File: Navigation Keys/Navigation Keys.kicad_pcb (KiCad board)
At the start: 2 copper layers, 22 parts, among them J1 Conn_01x19_Female, J2 Conn_01x19_Male

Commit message: Started wiring
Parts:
- moved D10 38.1 mm to (199.2, 127.8)
- moved D3 38.1 mm to (161.1, 127.8)
- moved MX_Left1 38.1 mm to (153.2, 127.8)
- moved MX_Right1 38.1 mm to (191.3, 127.8)
- renumbered MX_Right1 to MX_Left1, MX_Left1 to MX_Right1
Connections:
- D10 pad 1: ROW7 -> ROW8
- D3 pad 1: ROW7 -> ROW8
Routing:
- net COL4: track 0.00 -> 94.4 mm, vias 0 -> 8
- net COL5: track 0.00 -> 92.5 mm, vias 0 -> 8
- net GND: track 0.00 -> 85.4 mm, vias 0 -> 10
- net ROW9: track 0.00 -> 83.4 mm, vias 0 -> 8
- net COL6: track 0.00 -> 74.3 mm, vias 0 -> 8
- net COL10: track 0.00 -> 73.4 mm, vias 0 -> 6
- net COL9: track 0.00 -> 72.6 mm, vias 0 -> 6
- net COL7: track 0.00 -> 72.0 mm, vias 0 -> 8
- net COL8: track 0.00 -> 70.3 mm, vias 0 -> 6
- net COL3: track 0.00 -> 57.1 mm
- net COL2: track 0.00 -> 57.1 mm
- net COL1: track 0.00 -> 57.1 mm
- net ROW6: track 0.00 -> 44.5 mm, vias 0 -> 4
- net ROW8: track 0.00 -> 44.5 mm
- net ROW5: track 0.00 -> 44.5 mm, vias 0 -> 4
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
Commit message: Finished wiring and placement
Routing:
- net COL0: track 4.59 -> 108.1 mm, vias 0 -> 10
- net VCC: track 4.75 -> 107.3 mm, vias 0 -> 10
- net ROW8: track 44.5 -> 146.7 mm, vias 0 -> 2
- net +5V: track 4.65 -> 100.3 mm, vias 0 -> 6
- net ROW7: track 0.00 -> 92.9 mm, vias 0 -> 4
- net COL3: track 57.1 -> 148.1 mm, vias 0 -> 6
- net COL2: track 57.1 -> 143.3 mm, vias 0 -> 8
- net COL1: track 57.1 -> 143.1 mm, vias 0 -> 6
- net ROW5: track 44.5 -> 127.3 mm, vias 4 -> 10
- net ROW6: track 44.5 -> 92.9 mm, vias 4 -> 8
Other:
- board outline added: 73.8 x 76.2 mm

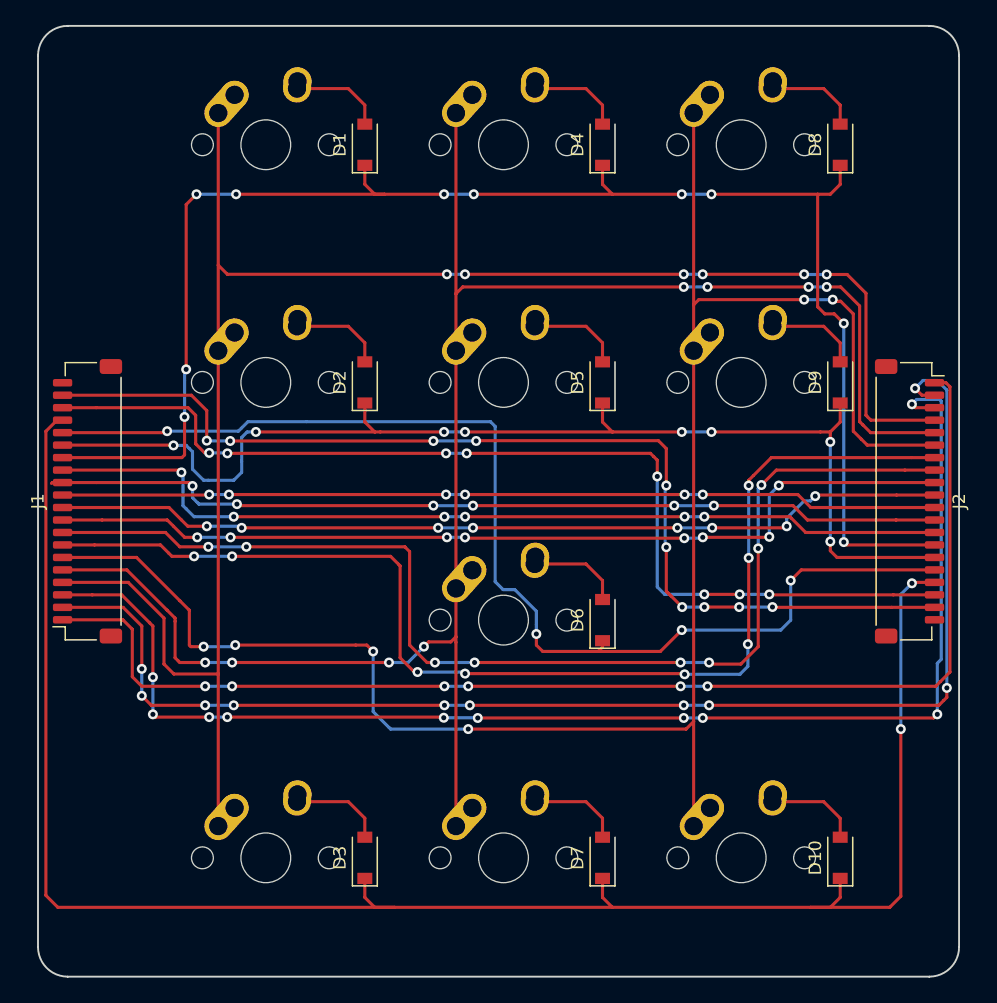
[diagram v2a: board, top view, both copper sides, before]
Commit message: Added ground plane
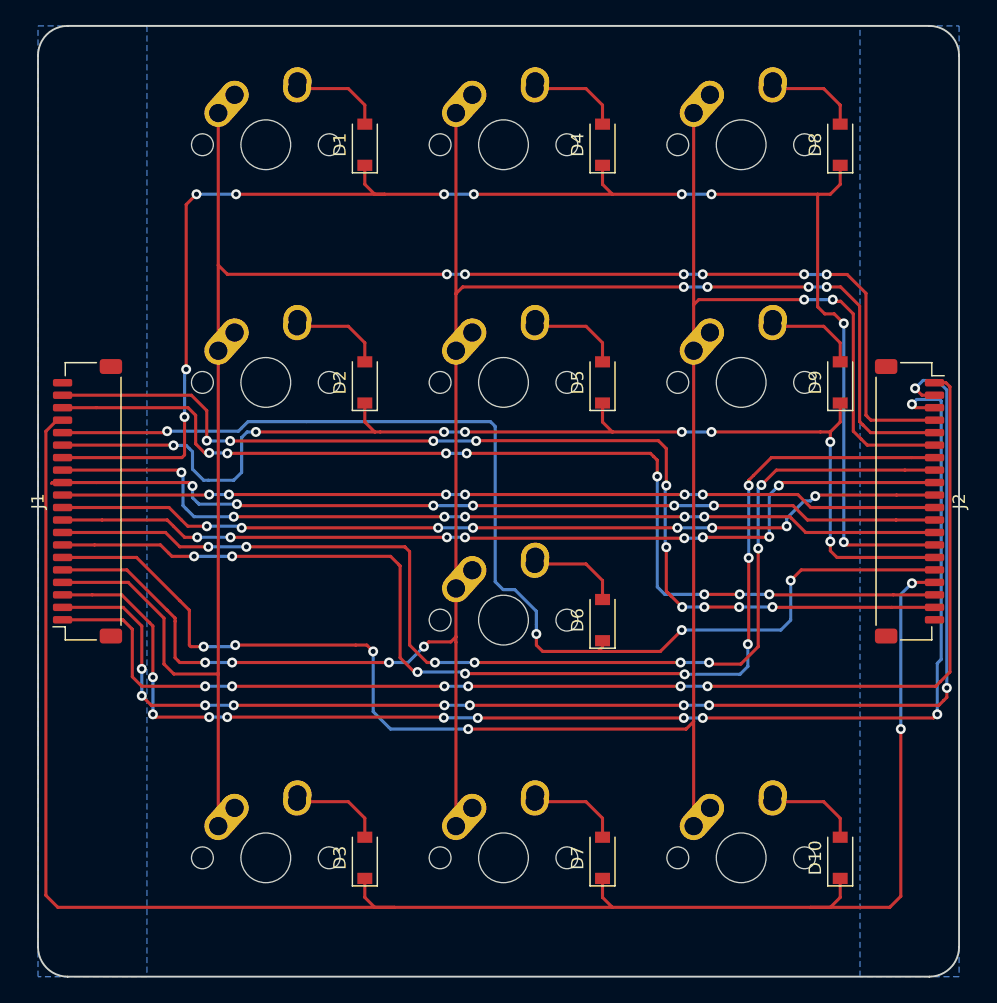
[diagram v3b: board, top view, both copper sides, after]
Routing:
- added copper zone on B.Cu, net GND
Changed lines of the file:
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@@
   (segment (start 185.293 102.902136) (end 185.203 102.812136) (width 0.25) (layer "B.Cu") (net 29))
   (segment (start 188.341 107.696) (end 186.563 107.696) (width 0.25) (layer "B.Cu") (net 29))
+  (zone (net 29) (net_name "GND") (layer "B.Cu") (hatch edge 0.508)
+    (connect_pads (clearance 0.508))
+    (min_thickness 0.254) (filled_areas_thickness no)
+    (fill yes (thermal_gap 0.508) (thermal_bridge_width 0.508))
+    (polygon
+      (pts
+        (xy 208.75625 137.31875)
+        (xy 200.81875 137.31875)
+        (xy 200.81875 61.11875)
+        (xy 208.75625 61.11875)
+      )
+    )
+  )
+  (zone (net 29) (net_name "GND") (layer "B.Cu") (hatch edge 0.508)
+    (connect_pads (clearance 0.508))
+    (min_thickness 0.254) (filled_areas_thickness no)
+    (fill yes (thermal_gap 0.508) (thermal_bridge_width 0.508))
+    (polygon
+      (pts
+        (xy 143.66875 137.31875)
+        (xy 134.9375 137.31875)
+        (xy 134.9375 61.11875)
+        (xy 143.66875 61.11875)
+      )
+    )
+  )
 )
